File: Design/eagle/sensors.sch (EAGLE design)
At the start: 10 parts

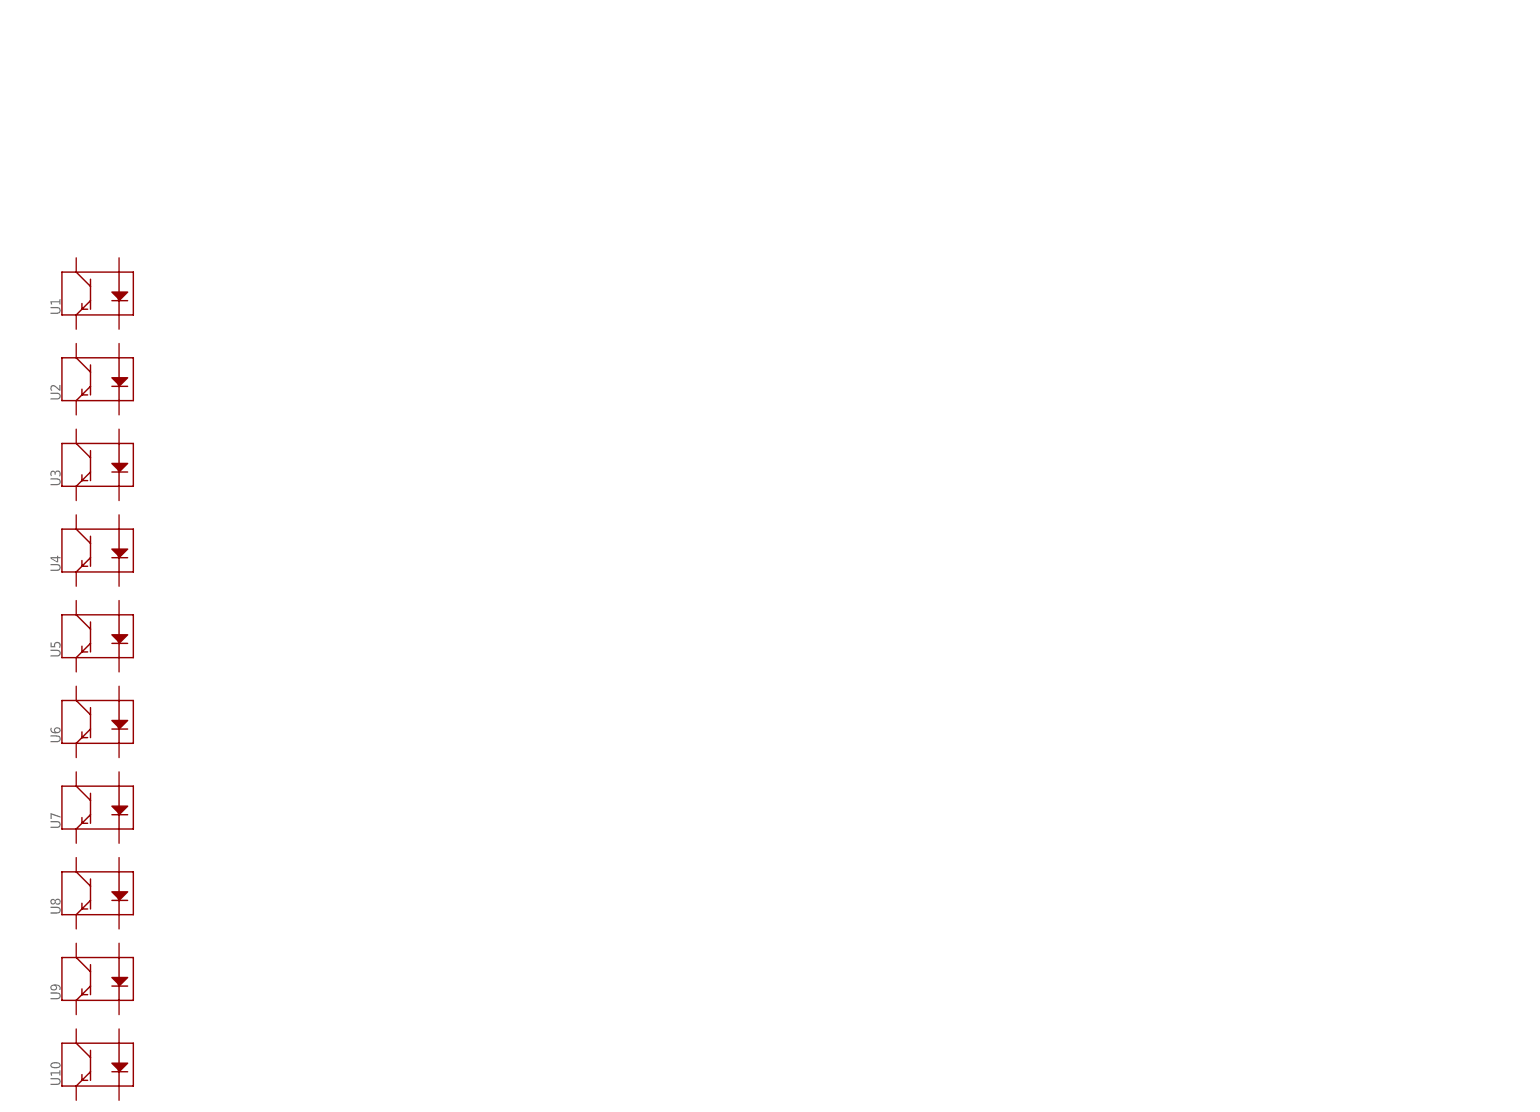
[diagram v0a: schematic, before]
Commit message: Finished sensor PCB + Analog MUX
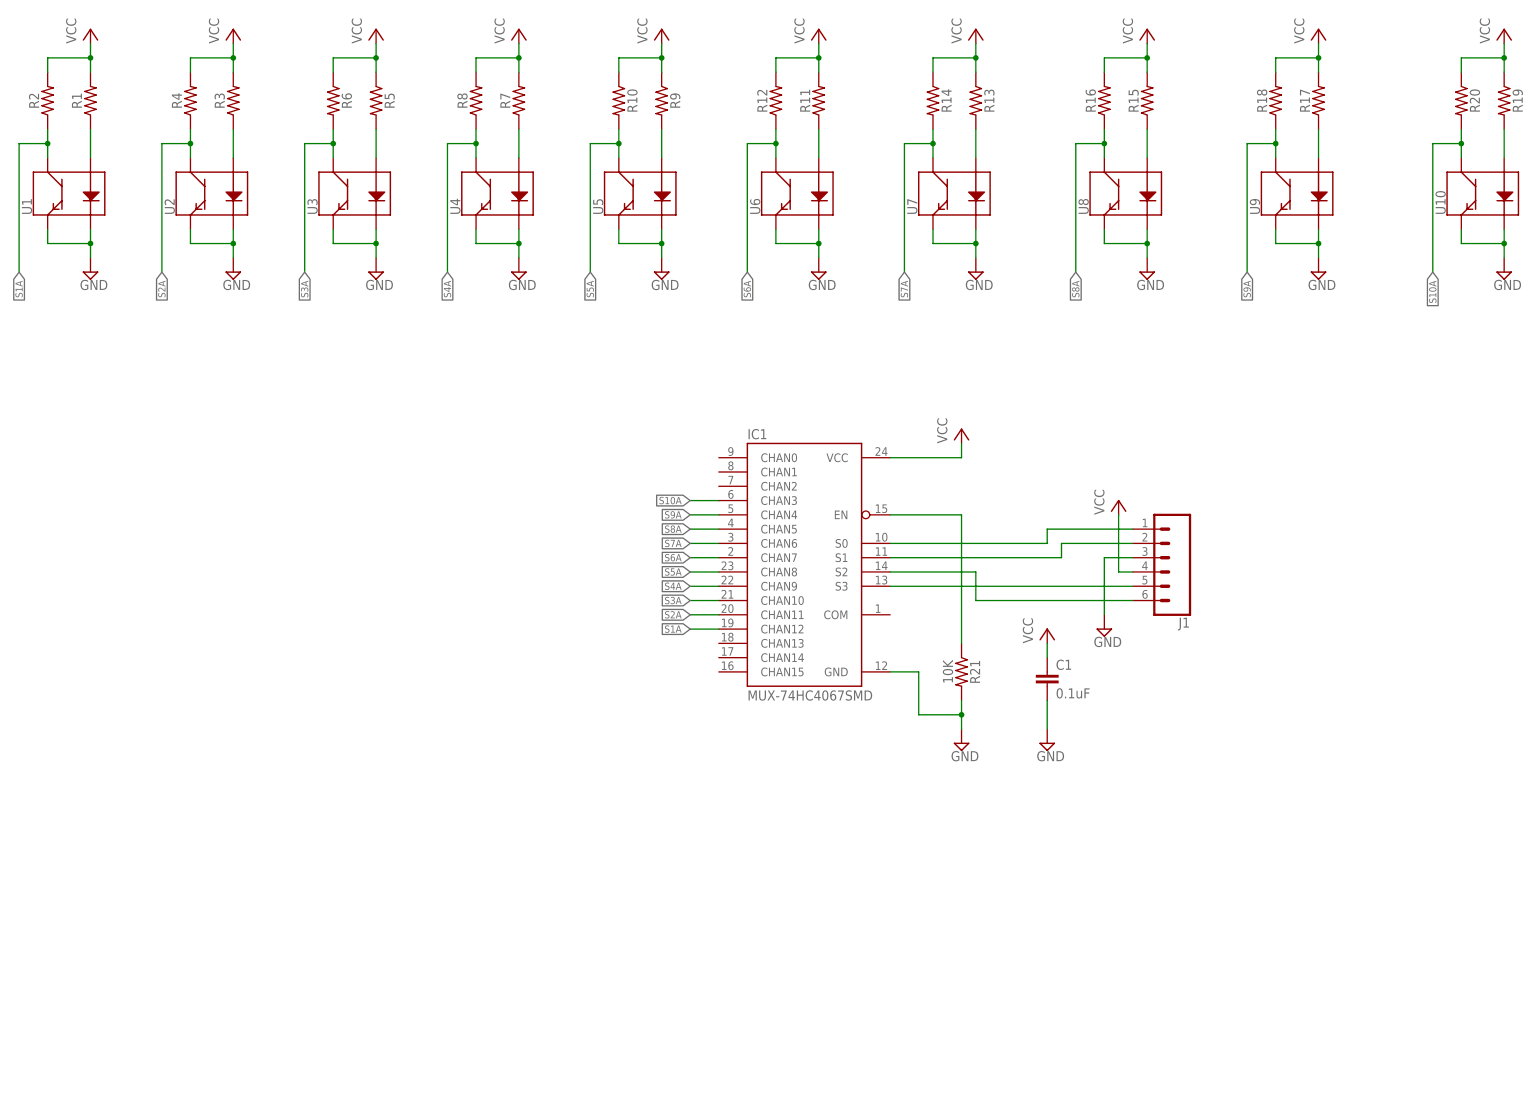
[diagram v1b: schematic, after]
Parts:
- added C1: 0.1uF, SparkFun-Capacitors:1.0UF-0805-25V-(+80/-20%)
- added IC1: MUX-74HC4067SMD, SeguidorLineasLbr:MUX-74HC4067SMD
- added J1: (no value), SparkFun-Connectors:CONN_06NO_SILK_NO_POP
- added R1, R10, R11, R12, R13, R14, R15, R16, R17, R18, R19, R2, R20, R3, R4, R5, R6, R7, R8, R9: (no value), SparkFun-Resistors:RESISTOR0805
- added R21: 10K, SparkFun-Resistors:RESISTOR0805
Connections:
- new net GND: C1.2, IC1.GND, J1.3, R21.2, U1.E, U1.K, U10.E, U10.K, U2.E, U2.K, U3.E, U3.K, U4.E, U4.K, U5.E, U5.K, U6.E, U6.K, U7.E, U7.K, U8.E, U8.K, U9.E, U9.K
- new net N$1: R1.1, U1.A
- new net N$10: IC1.S1, J1.2
- new net N$11: R11.1, U6.A
- new net N$13: R13.2, U7.A
- new net N$15: R15.1, U8.A
- new net N$17: R17.1, U9.A
- new net N$19: R19.2, U10.A
- new net N$2: IC1.S3, J1.5
- new net N$3: R3.1, U2.A
- new net N$4: IC1.EN, R21.1
- new net N$5: R5.2, U3.A
- new net N$6: IC1.S2, J1.6
- new net N$7: R7.1, U4.A
- new net N$8: IC1.S0, J1.1
- new net N$9: R9.2, U5.A
- new net S10A: IC1.CHAN3, R20.2, U10.C
- new net S1A: IC1.CHAN12, R2.1, U1.C
- new net S2A: IC1.CHAN11, R4.1, U2.C
- new net S3A: IC1.CHAN10, R6.2, U3.C
- new net S4A: IC1.CHAN9, R8.1, U4.C
- new net S5A: IC1.CHAN8, R10.2, U5.C
- new net S6A: IC1.CHAN7, R12.1, U6.C
- new net S7A: IC1.CHAN6, R14.2, U7.C
- new net S8A: IC1.CHAN5, R16.1, U8.C
- new net S9A: IC1.CHAN4, R18.1, U9.C
- new net VCC: C1.1, IC1.VCC, J1.4, R1.2, R10.1, R11.2, R12.2, R13.1, R14.1, R15.2, R16.2, R17.2, R18.2, R19.1, R2.2, R20.1, R3.2, R4.2, R5.1, R6.1, R7.2, R8.2, R9.1
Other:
- moved on the sheet: U1, U10, U2, U3, U4, U5, U6, U7, U8, U9

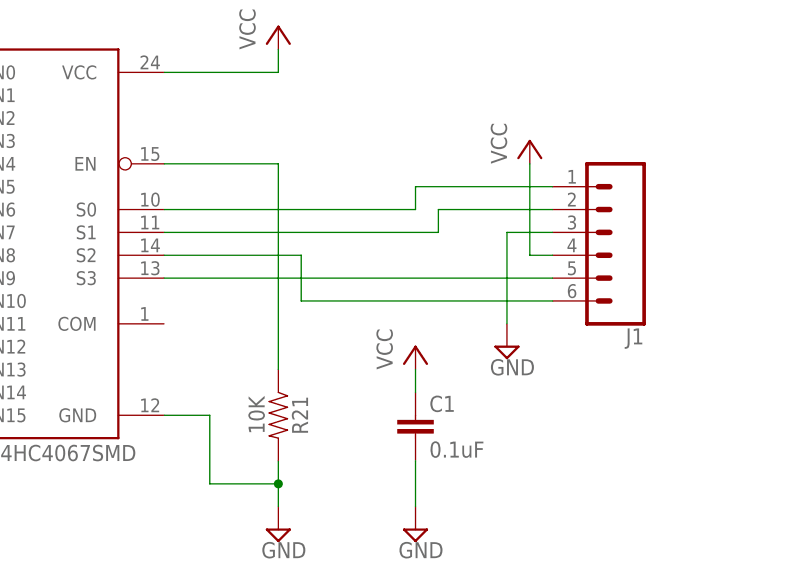
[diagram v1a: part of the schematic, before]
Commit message: Fixed missing COM line from analog MUX
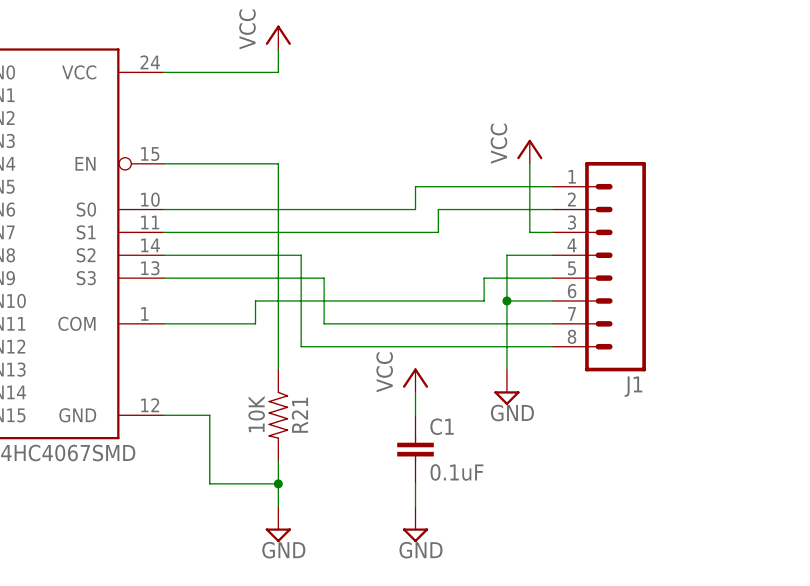
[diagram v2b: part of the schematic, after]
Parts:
- J1: device SparkFun-Connectors:CONN_06NO_SILK_NO_POP -> SparkFun-Connectors:M08
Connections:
- new net N$12: IC1.COM, J1.5
- net GND: now also J1.4, J1.6; no longer J1.3
- net N$2: now also J1.7; no longer J1.5
- net N$6: now also J1.8; no longer J1.6
- net VCC: now also J1.3; no longer J1.4
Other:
- moved on the sheet: C1
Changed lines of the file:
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@@
 <?xml version="1.0" encoding="utf-8"?>
 <!DOCTYPE eagle SYSTEM "eagle.dtd">
-<eagle version="7.7.0">
+<eagle version="7.4.0">
 <drawing>
 <settings>
@@
 <part name="P+12" library="supply1" deviceset="VCC" device=""/>
 <part name="SUPPLY12" library="supply2" deviceset="GND" device=""/>
-<part name="J1" library="SparkFun-Connectors" deviceset="CONN_06" device="NO_SILK_NO_POP"/>
+<part name="J1" library="SparkFun-Connectors" deviceset="M08" device=""/>
 <part name="SUPPLY13" library="supply2" deviceset="GND" device=""/>
 <part name="P+13" library="supply1" deviceset="VCC" device=""/>
@@
 <instance part="R21" gate="G$1" x="182.88" y="30.48" rot="R270"/>
 <instance part="P+11" gate="VCC" x="182.88" y="73.66"/>
-<instance part="C1" gate="G$1" x="198.12" y="27.94"/>
-<instance part="P+12" gate="VCC" x="198.12" y="38.1"/>
+<instance part="C1" gate="G$1" x="198.12" y="25.4"/>
+<instance part="P+12" gate="VCC" x="198.12" y="35.56"/>
 <instance part="SUPPLY12" gate="GND" x="198.12" y="17.78"/>
-<instance part="J1" gate="G$1" x="218.44" y="50.8" rot="R180"/>
-<instance part="SUPPLY13" gate="GND" x="208.28" y="38.1"/>
+<instance part="J1" gate="G$1" x="218.44" y="48.26" rot="R180"/>
+<instance part="SUPPLY13" gate="GND" x="208.28" y="33.02"/>
 <instance part="P+13" gate="VCC" x="210.82" y="60.96"/>
 </instances>
@@
 <pinref part="P+12" gate="VCC" pin="VCC"/>
 <pinref part="C1" gate="G$1" pin="1"/>
-<wire x1="198.12" y1="35.56" x2="198.12" y2="33.02" width="0.1524" layer="91"/>
-</segment>
-<segment>
-<pinref part="J1" gate="G$1" pin="4"/>
+<wire x1="198.12" y1="33.02" x2="198.12" y2="30.48" width="0.1524" layer="91"/>
+</segment>
+<segment>
 <pinref part="P+13" gate="VCC" pin="VCC"/>
-<wire x1="213.36" y1="48.26" x2="210.82" y2="48.26" width="0.1524" layer="91"/>
-<wire x1="210.82" y1="48.26" x2="210.82" y2="58.42" width="0.1524" layer="91"/>
+<pinref part="J1" gate="G$1" pin="3"/>
+<wire x1="210.82" y1="58.42" x2="210.82" y2="50.8" width="0.1524" layer="91"/>
+<wire x1="210.82" y1="50.8" x2="213.36" y2="50.8" width="0.1524" layer="91"/>
 </segment>
 </net>
@@
 <pinref part="C1" gate="G$1" pin="2"/>
 <pinref part="SUPPLY12" gate="GND" pin="GND"/>
-<wire x1="198.12" y1="25.4" x2="198.12" y2="20.32" width="0.1524" layer="91"/>
-</segment>
-<segment>
-<pinref part="J1" gate="G$1" pin="3"/>
+<wire x1="198.12" y1="22.86" x2="198.12" y2="20.32" width="0.1524" layer="91"/>
+</segment>
+<segment>
 <pinref part="SUPPLY13" gate="GND" pin="GND"/>
-<wire x1="213.36" y1="50.8" x2="208.28" y2="50.8" width="0.1524" layer="91"/>
-<wire x1="208.28" y1="50.8" x2="208.28" y2="40.64" width="0.1524" layer="91"/>
+<pinref part="J1" gate="G$1" pin="4"/>
+<wire x1="208.28" y1="35.56" x2="208.28" y2="43.18" width="0.1524" layer="91"/>
+<wire x1="208.28" y1="43.18" x2="208.28" y2="48.26" width="0.1524" layer="91"/>
+<wire x1="208.28" y1="48.26" x2="213.36" y2="48.26" width="0.1524" layer="91"/>
+<pinref part="J1" gate="G$1" pin="6"/>
+<wire x1="213.36" y1="43.18" x2="208.28" y2="43.18" width="0.1524" layer="91"/>
+<junction x="208.28" y="43.18"/>
 </segment>
 </net>
@@
 </segment>
 </net>
-<net name="N$2" class="0">
-<segment>
-<pinref part="IC1" gate="G$1" pin="S3"/>
-<pinref part="J1" gate="G$1" pin="5"/>
-<wire x1="170.18" y1="45.72" x2="213.36" y2="45.72" width="0.1524" layer="91"/>
-</segment>
-</net>
 <net name="N$6" class="0">
 <segment>
-<pinref part="J1" gate="G$1" pin="6"/>
-<wire x1="213.36" y1="43.18" x2="185.42" y2="43.18" width="0.1524" layer="91"/>
-<wire x1="185.42" y1="43.18" x2="185.42" y2="48.26" width="0.1524" layer="91"/>
+<wire x1="185.42" y1="38.1" x2="185.42" y2="48.26" width="0.1524" layer="91"/>
 <pinref part="IC1" gate="G$1" pin="S2"/>
 <wire x1="185.42" y1="48.26" x2="170.18" y2="48.26" width="0.1524" layer="91"/>
+<pinref part="J1" gate="G$1" pin="8"/>
+<wire x1="185.42" y1="38.1" x2="213.36" y2="38.1" width="0.1524" layer="91"/>
 </segment>
 </net>
@@
 </segment>
 </net>
+<net name="N$2" class="0">
+<segment>
+<pinref part="IC1" gate="G$1" pin="S3"/>
+<wire x1="170.18" y1="45.72" x2="187.96" y2="45.72" width="0.1524" layer="91"/>
+<pinref part="J1" gate="G$1" pin="7"/>
+<wire x1="187.96" y1="45.72" x2="187.96" y2="40.64" width="0.1524" layer="91"/>
+<wire x1="187.96" y1="40.64" x2="213.36" y2="40.64" width="0.1524" layer="91"/>
+</segment>
+</net>
+<net name="N$12" class="0">
+<segment>
+<pinref part="IC1" gate="G$1" pin="COM"/>
+<wire x1="170.18" y1="40.64" x2="180.34" y2="40.64" width="0.1524" layer="91"/>
+<wire x1="180.34" y1="40.64" x2="180.34" y2="43.18" width="0.1524" layer="91"/>
+<wire x1="180.34" y1="43.18" x2="205.74" y2="43.18" width="0.1524" layer="91"/>
+<pinref part="J1" gate="G$1" pin="5"/>
+<wire x1="205.74" y1="43.18" x2="205.74" y2="45.72" width="0.1524" layer="91"/>
+<wire x1="205.74" y1="45.72" x2="213.36" y2="45.72" width="0.1524" layer="91"/>
+</segment>
+</net>
